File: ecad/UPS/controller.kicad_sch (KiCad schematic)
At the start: 11 parts, among them J2 Conn_01x05_Socket, SW1 SW_Push, U1 STM32L152RCT6

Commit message: assign footprints
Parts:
- renumbered decouplingcapateachVDDpin to decouplingcapateachVDDpin1, pull-upresistoronSCL to pull-upresistoronSCL1, pull-upresistoronSDA to pull-upresistoronSDA1
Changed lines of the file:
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@@
 		(on_board yes)
 		(dnp no)
-		(property "Reference" "#PWR030"
+		(property "Reference" "#PWR0115"
 			(at 86.36 78.74 0)
 			(effects
@@
 			(project "controller"
 				(path "/9d92b60a-4a6b-449c-b462-cab19e69d38c/1d606685-c4fd-4b8c-9a71-b1626d28c437"
-					(reference "#PWR030")
+					(reference "#PWR0115")
 					(unit 1)
 				)
@@
 		(on_board yes)
 		(dnp no)
-		(property "Reference" "#PWR031"
+		(property "Reference" "#PWR0114"
 			(at 86.36 93.98 0)
 			(effects
@@
 			(project "controller"
 				(path "/9d92b60a-4a6b-449c-b462-cab19e69d38c/1d606685-c4fd-4b8c-9a71-b1626d28c437"
-					(reference "#PWR031")
+					(reference "#PWR0114")
 					(unit 1)
 				)
@@
 		(on_board yes)
 		(dnp no)
-		(property "Reference" "#PWR012"
+		(property "Reference" "#PWR0109"
 			(at 120.65 135.89 0)
 			(effects
@@
 			(project "controller"
 				(path "/9d92b60a-4a6b-449c-b462-cab19e69d38c/1d606685-c4fd-4b8c-9a71-b1626d28c437"
-					(reference "#PWR012")
+					(reference "#PWR0109")
 					(unit 1)
 				)
@@
 		(on_board yes)
 		(dnp no)
-		(property "Reference" "#PWR013"
+		(property "Reference" "#PWR0113"
 			(at 120.65 29.21 0)
 			(effects
@@
 			(project "controller"
 				(path "/9d92b60a-4a6b-449c-b462-cab19e69d38c/1d606685-c4fd-4b8c-9a71-b1626d28c437"
-					(reference "#PWR013")
+					(reference "#PWR0113")
 					(unit 1)
 				)
@@
 		(on_board yes)
 		(dnp no)
-		(property "Reference" "#PWR04"
+		(property "Reference" "#PWR0111"
 			(at 175.26 125.73 0)
 			(effects
@@
 			(project "controller"
 				(path "/9d92b60a-4a6b-449c-b462-cab19e69d38c/1d606685-c4fd-4b8c-9a71-b1626d28c437"
-					(reference "#PWR04")
+					(reference "#PWR0111")
 					(unit 1)
 				)
@@
 		(on_board yes)
 		(dnp no)
-		(property "Reference" "#PWR05"
+		(property "Reference" "#PWR0112"
 			(at 175.26 99.06 0)
 			(effects
@@
 			(project "controller"
 				(path "/9d92b60a-4a6b-449c-b462-cab19e69d38c/1d606685-c4fd-4b8c-9a71-b1626d28c437"
-					(reference "#PWR05")
+					(reference "#PWR0112")
 					(unit 1)
 				)
@@
 		(on_board yes)
 		(dnp no)
-		(property "Reference" "#PWR024"
+		(property "Reference" "#PWR0116"
 			(at 77.47 55.88 0)
 			(effects
@@
 			(project "controller"
 				(path "/9d92b60a-4a6b-449c-b462-cab19e69d38c/1d606685-c4fd-4b8c-9a71-b1626d28c437"
-					(reference "#PWR024")
+					(reference "#PWR0116")
 					(unit 1)
 				)
@@
 		(dnp no)
 		(fields_autoplaced yes)
-		(property "Reference" "pull-upresistoronSCL"
+		(property "Reference" "pull-upresistoronSCL1"
 			(at 68.58 97.79 90)
 			(effects
@@
 			(project ""
 				(path "/9d92b60a-4a6b-449c-b462-cab19e69d38c/1d606685-c4fd-4b8c-9a71-b1626d28c437"
-					(reference "pull-upresistoronSCL")
+					(reference "pull-upresistoronSCL1")
 					(unit 1)
 				)
@@
 		(dnp no)
 		(fields_autoplaced yes)
-		(property "Reference" "decouplingcapateachVDDpin"
+		(property "Reference" "decouplingcapateachVDDpin1"
 			(at 93.98 134.6199 0)
 			(effects
@@
 			(project ""
 				(path "/9d92b60a-4a6b-449c-b462-cab19e69d38c/1d606685-c4fd-4b8c-9a71-b1626d28c437"
-					(reference "decouplingcapateachVDDpin")
+					(reference "decouplingcapateachVDDpin1")
 					(unit 1)
 				)
@@
 		(on_board yes)
 		(dnp no)
-		(property "Reference" "#PWR03"
+		(property "Reference" "#PWR0110"
 			(at 161.29 133.35 0)
 			(effects
@@
 			(project "controller"
 				(path "/9d92b60a-4a6b-449c-b462-cab19e69d38c/1d606685-c4fd-4b8c-9a71-b1626d28c437"
-					(reference "#PWR03")
+					(reference "#PWR0110")
 					(unit 1)
 				)
@@
 		(dnp no)
 		(fields_autoplaced yes)
-		(property "Reference" "pull-upresistoronSDA"
+		(property "Reference" "pull-upresistoronSDA1"
 			(at 88.9 100.33 90)
 			(effects
@@
 			(project ""
 				(path "/9d92b60a-4a6b-449c-b462-cab19e69d38c/1d606685-c4fd-4b8c-9a71-b1626d28c437"
-					(reference "pull-upresistoronSDA")
-					(unit 1)
-				)
+					(reference "pull-upresistoronSDA1")
+					(unit 1)
+				)

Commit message: Fix duplicate component names.
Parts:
- removed C1: 100nF, Capacitor_SMD:C_0603_1608Metric, symbol Device:C_Small
- removed D1: LED, LED_SMD:LED_0805_2012Metric, symbol Device:LED
- removed R1, R2: 10K, Resistor_SMD:R_0805_2012Metric, symbol Device:R_Small
- removed R7: 1.5K, Resistor_SMD:R_0805_2012Metric, symbol Device:R_Small
- added C4: 100nF, Capacitor_SMD:C_0603_1608Metric, symbol Device:C_Small
- added D6: LED, LED_SMD:LED_0805_2012Metric, symbol Device:LED
- added R28, R29: 10K, Resistor_SMD:R_0805_2012Metric, symbol Device:R_Small
- added R33: 1.5K, Resistor_SMD:R_0805_2012Metric, symbol Device:R_Small
- renumbered J2 to J4, U1 to U4
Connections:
- net +3.3V: now also R29.1
- net GND: now also C4.2, R28.2, R33.2
- net NRST: now also C4.1, R29.2
- net at U4.20 (PA4): now also D6.2 (A)
- net at U4.60 (BOOT0): now also R28.1
- new net: D6.1 (K), R33.1

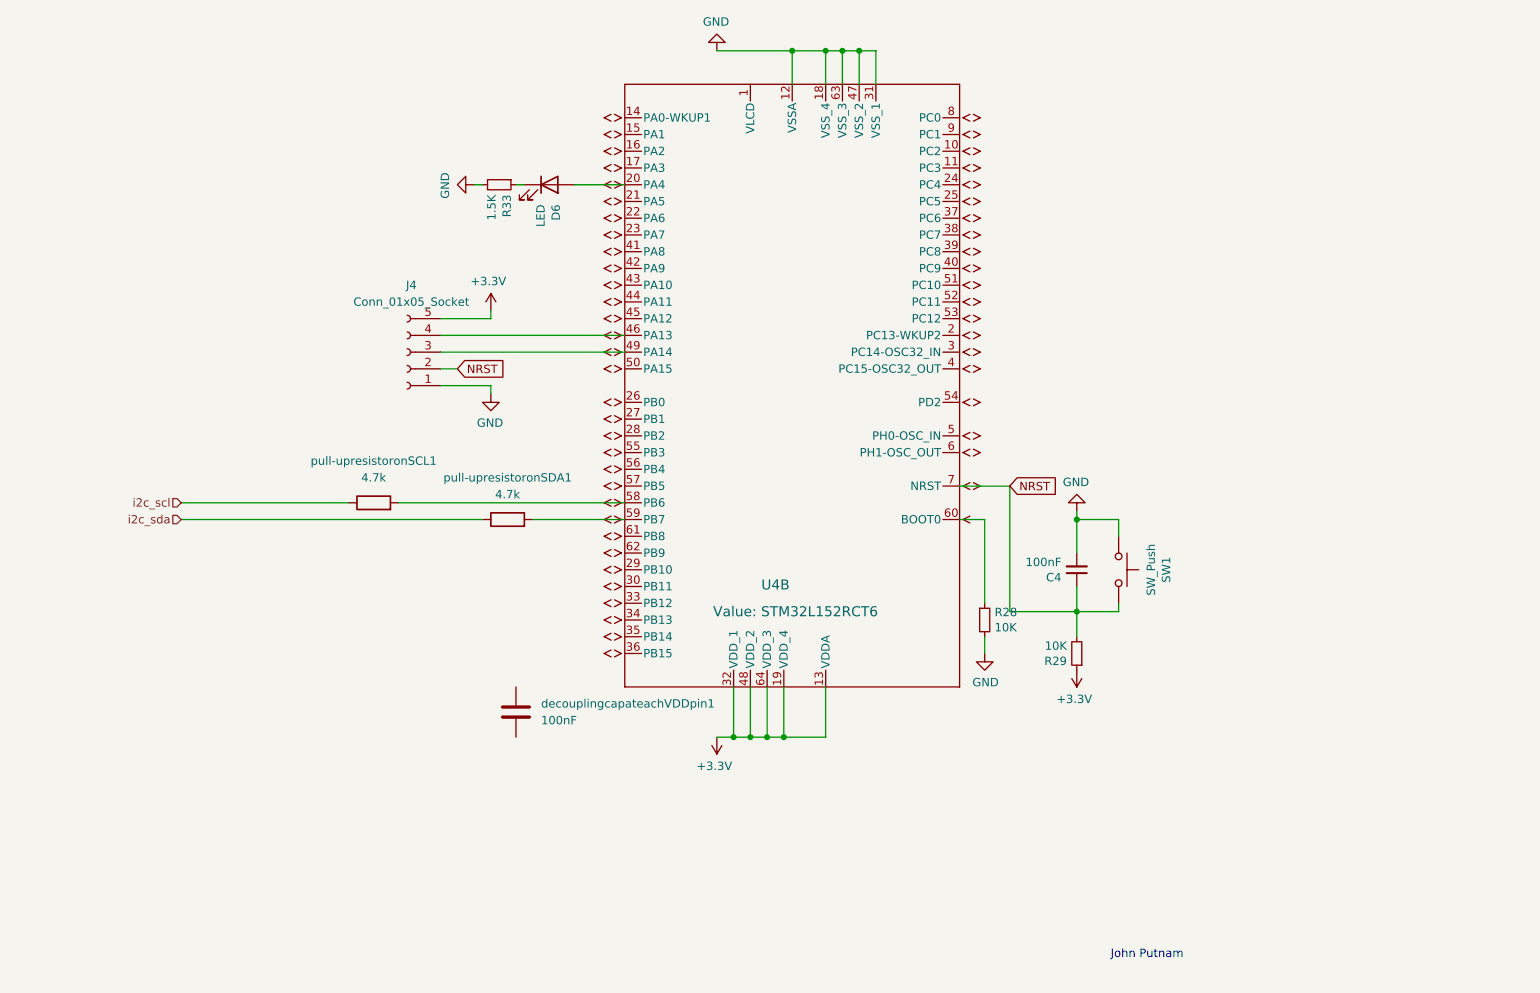
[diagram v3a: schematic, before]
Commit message: mcu fixed
fixed i2c and gpio and boot and decoupler and add 3.3 regulator.
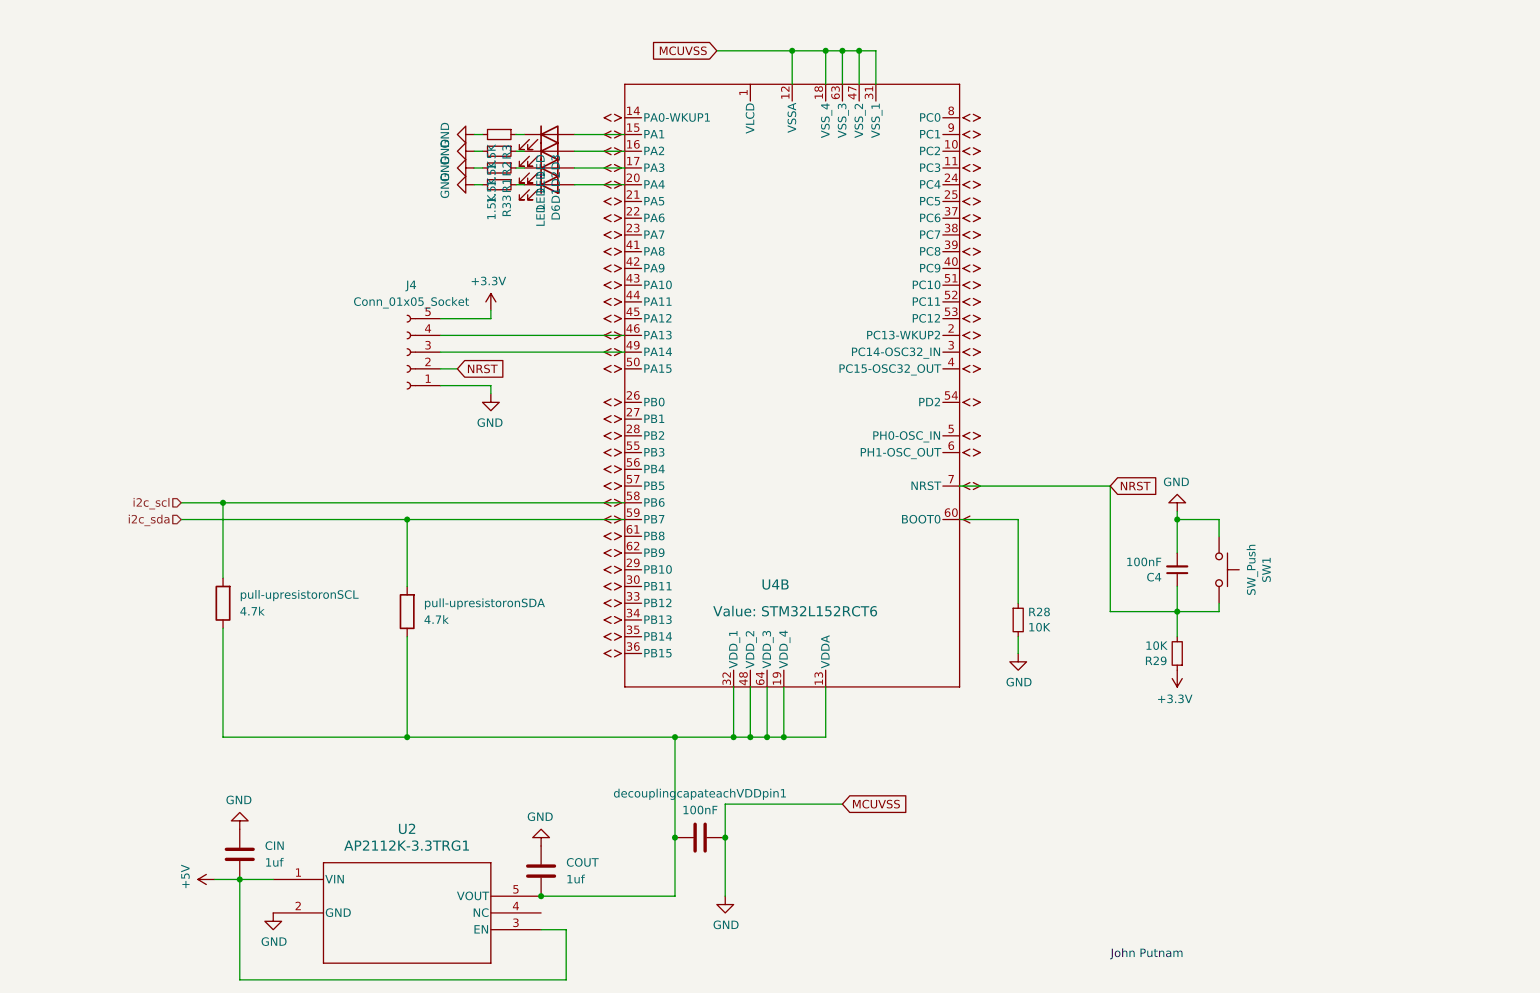
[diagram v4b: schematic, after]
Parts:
- added CIN, COUT: 1uf, symbol Device:C
- added D1, D2, D3: LED, LED_SMD:LED_0805_2012Metric, symbol Device:LED
- added R1, R2, R3: 1.5K, Resistor_SMD:R_0805_2012Metric, symbol Device:R_Small
- added U2: AP2112K-3.3TRG1, SOT_RG1_DIO, symbol UPS:AP2112K-3.3TRG1
- renumbered pull-upresistoronSCL1 to pull-upresistoronSCL, pull-upresistoronSDA1 to pull-upresistoronSDA
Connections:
- net +3.3V: no longer U4.13 (VDDA), U4.19 (VDD_4), U4.32 (VDD_1), U4.48 (VDD_2), U4.64 (VDD_3)
- net GND: now also decouplingcapateachVDDpin1.2, CIN.2, COUT.2, R1.2, R2.2, R3.2, U2.2 (GND)
- net i2c_scl: now also U4.58 (PB6), pull-upresistoronSCL.2; no longer pull-upresistoronSCL.1
- net i2c_sda: now also U4.59 (PB7), pull-upresistoronSDA.2; no longer pull-upresistoronSDA.1
- net at decouplingcapateachVDDpin1.1: now also U4.13 (VDDA), U4.19 (VDD_4), U4.32 (VDD_1), U4.48 (VDD_2), U4.64 (VDD_3), pull-upresistoronSCL.1, pull-upresistoronSDA.1, COUT.1, U2.5 (VOUT)
- net at U4.15 (PA1): now also D3.2 (A)
- net at U4.16 (PA2): now also D2.2 (A)
- net at U4.17 (PA3): now also D1.2 (A)
- new net: D2.1 (K), R2.1
- new net: D1.1 (K), R1.1
- new net: D3.1 (K), R3.1
- new net +5V: CIN.1, U2.1 (VIN), U2.3 (EN)
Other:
- moved on the sheet: C4, R28, R29, SW1, decouplingcapateachVDDpin1, pull-upresistoronSCL, pull-upresistoronSDA

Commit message: more gpio
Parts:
- removed R28: 10K, Resistor_SMD:R_0805_2012Metric, symbol Device:R_Small
- added C1: 0.1uf, Capacitor_SMD:C_0603_1608Metric, symbol Device:C_Small
- added R4: 10K, Resistor_SMD:R_0805_2012Metric, symbol Device:R_Small
- added R6, R7: R, symbol Device:R
- added SW2: SW_Push, Button_Switch_SMD:SW_SPST_B3U-1000P-B, symbol Switch:SW_Push
- added decouplingcapateachVDDpin1, decouplingcapateachVDDpin2, decouplingcapateachVDDpin3, decouplingcapateachVDDpin4: 100nF, symbol Device:C
- added pull-upresistoronSDA1, pull-upresistoronSDA2, pull-upresistoronSDA3, pull-upresistoronSDA4: 4.7k, symbol Device:R
- C2: renamed from C4; value 100nF -> 0.1uf
- renumbered D6 to D?, J4 to J2, R29 to R5, R33 to R?, U4 to U1, decouplingcapateachVDDpin1 to decouplingcapateachVDDpin, pull-upresistoronSCL to pull-upresistors
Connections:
- net +3.3V: no longer R5.1
- net GND: now also decouplingcapateachVDDpin.1, C1.2, R7.2, SW2.1, decouplingcapateachVDDpin1.1, decouplingcapateachVDDpin2.1, decouplingcapateachVDDpin3.1, decouplingcapateachVDDpin4.1; no longer decouplingcapateachVDDpin.2
- net at COUT.1, U1.13 (VDDA), U1.19 (VDD_4)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: now also decouplingcapateachVDDpin.2, R6.2, decouplingcapateachVDDpin1.2, decouplingcapateachVDDpin2.2, decouplingcapateachVDDpin3.2, decouplingcapateachVDDpin4.2, pull-upresistoronSDA1.1, pull-upresistoronSDA2.1, pull-upresistoronSDA3.1, pull-upresistoronSDA4.1; no longer decouplingcapateachVDDpin.1
- net at D?.2 (A): no longer U1.20 (PA4)
- net at D2.2 (A): no longer U1.16 (PA2)
- net at D3.2 (A): no longer U1.15 (PA1)
- net at D1.2 (A): no longer U1.17 (PA3)
- net at U1.60 (BOOT0): now also C1.1, R4.2, SW2.2
- net PROCHOT_N: now reaches U1.14 (PA0-WKUP1)
- net PROCHOT_N: now also pull-upresistoronSDA1.2
- net OTG/VAP: now reaches U1.26 (PB0)
- net OTG/VAP: now also pull-upresistoronSDA3.2
- net cmp_out: now reaches U1.27 (PB1)
- net cmp_out: now also pull-upresistoronSDA4.2
- new net 3.3V: R4.1, R5.1
- new net CMPIN: R6.1, R7.1
- new net chrg_ok: U1.15 (PA1), pull-upresistoronSDA2.2
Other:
- moved on the sheet: C2, D1, D2, D3, D?, R1, R2, R3, R5, R?, SW1, decouplingcapateachVDDpin

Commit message: more gpio
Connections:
- net OTG/VAP: now also U1.22 (PA6); no longer U1.26 (PB0)
- net cmp_out: now also U1.23 (PA7); no longer U1.27 (PB1)
- net i2c_scl: now also U1.61 (PB8); no longer U1.58 (PB6)
- net i2c_sda: now also U1.62 (PB9); no longer U1.59 (PB7)
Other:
- moved on the sheet: D1, D2, D3, D?, J2, R1, R2, R3, R?

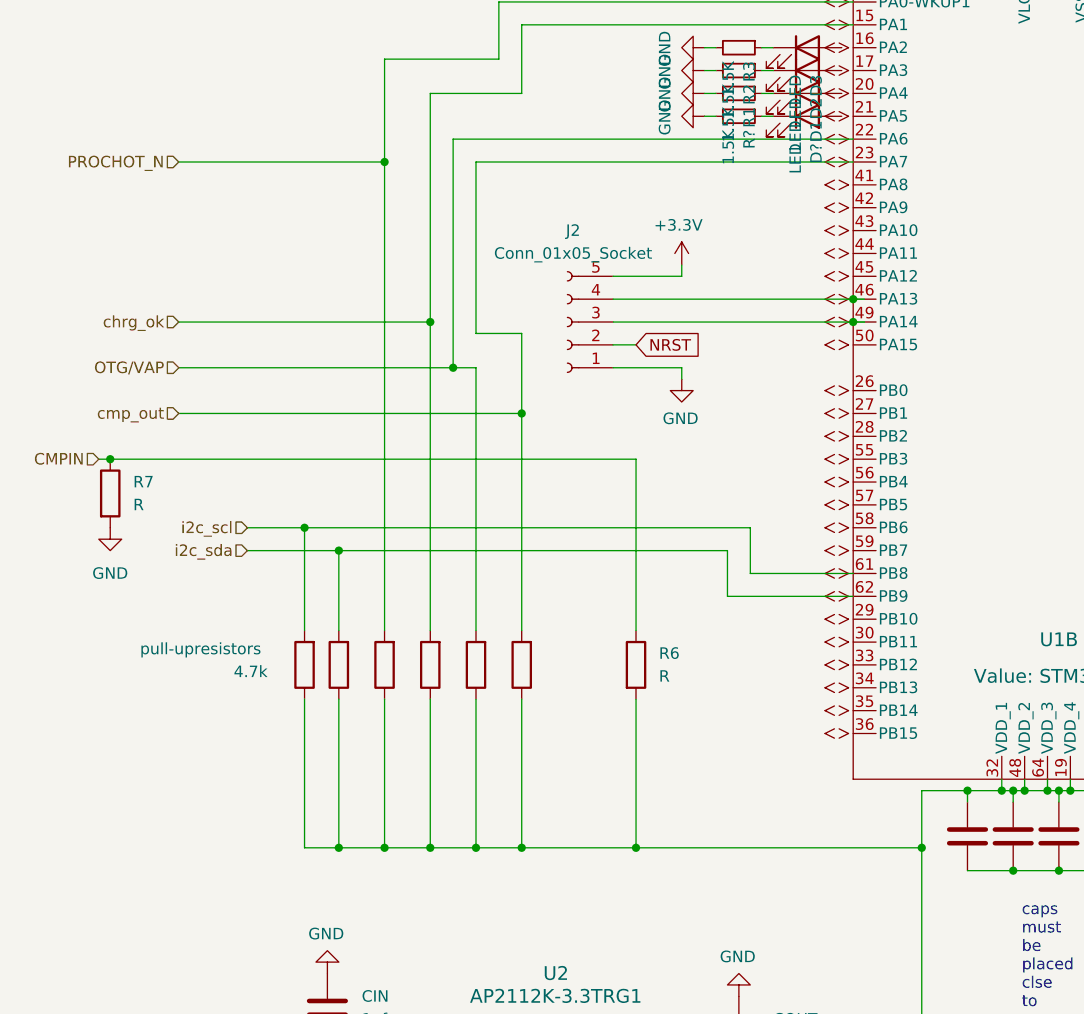
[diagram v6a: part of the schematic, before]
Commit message: resistor change
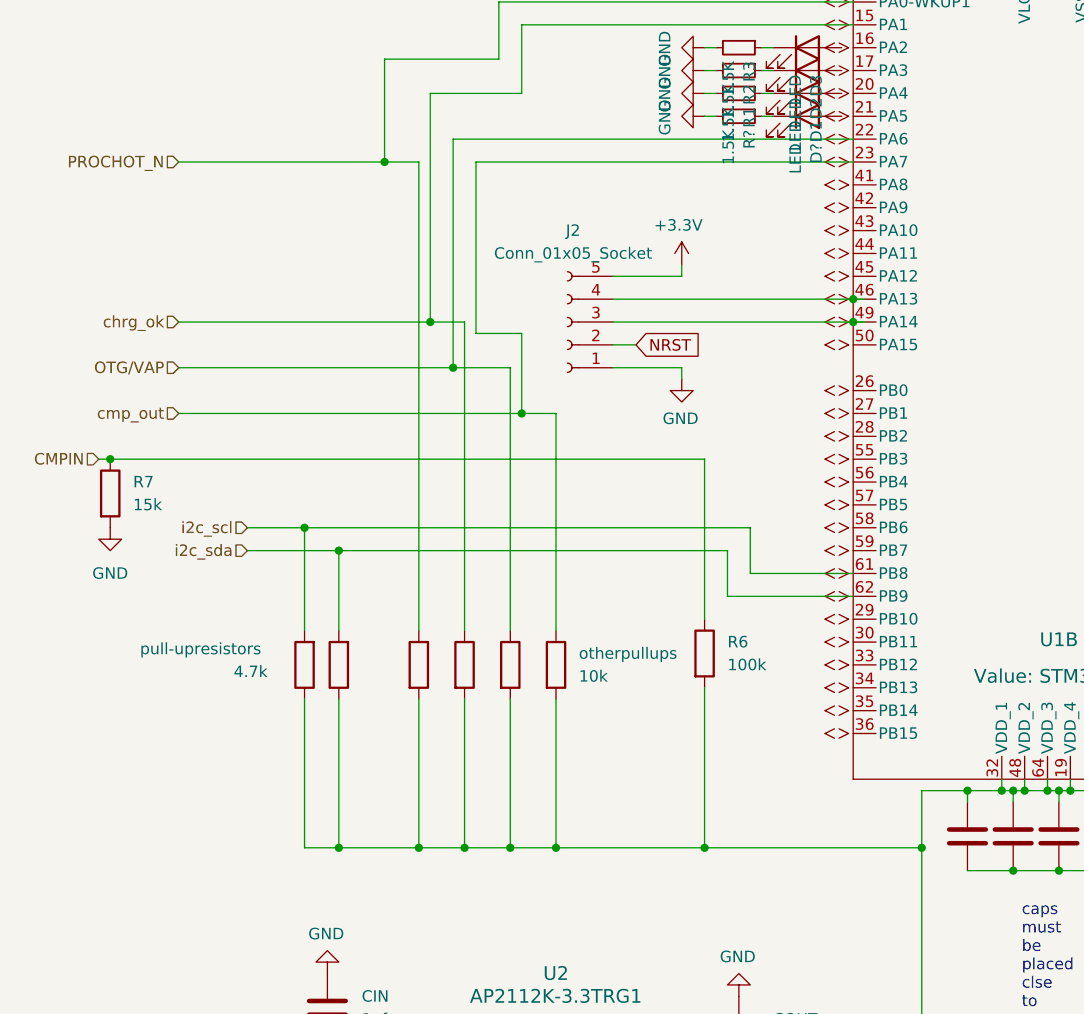
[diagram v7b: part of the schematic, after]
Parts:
- removed pull-upresistoronSDA1, pull-upresistoronSDA2, pull-upresistoronSDA3, pull-upresistoronSDA4: 4.7k, symbol Device:R
- added otherpullups, otherpullups1, otherpullups2, otherpullups3: 10k, symbol Device:R
- R6: value R -> 100k
- R7: value R -> 15k
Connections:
- net OTG/VAP: now also otherpullups1.1
- net PROCHOT_N: now also otherpullups3.1
- net chrg_ok: now also otherpullups2.1
- net cmp_out: now also otherpullups.1
- net at COUT.1, R6.2, U1.13 (VDDA)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: now also otherpullups.2, otherpullups1.2, otherpullups2.2, otherpullups3.2
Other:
- moved on the sheet: R6
